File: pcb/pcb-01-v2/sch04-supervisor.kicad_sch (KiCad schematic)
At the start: 22 parts, among them J5 B5B-PH-K-S(LF)(SN), Q4 BC847BDW1T1G, SW1 PTS645SK43SMTR92LFS, SW2 PTS645SK43SMTR92LFS, U12 TMP1075DGKR, U2 ESP32-C6-WROOM-1-N8

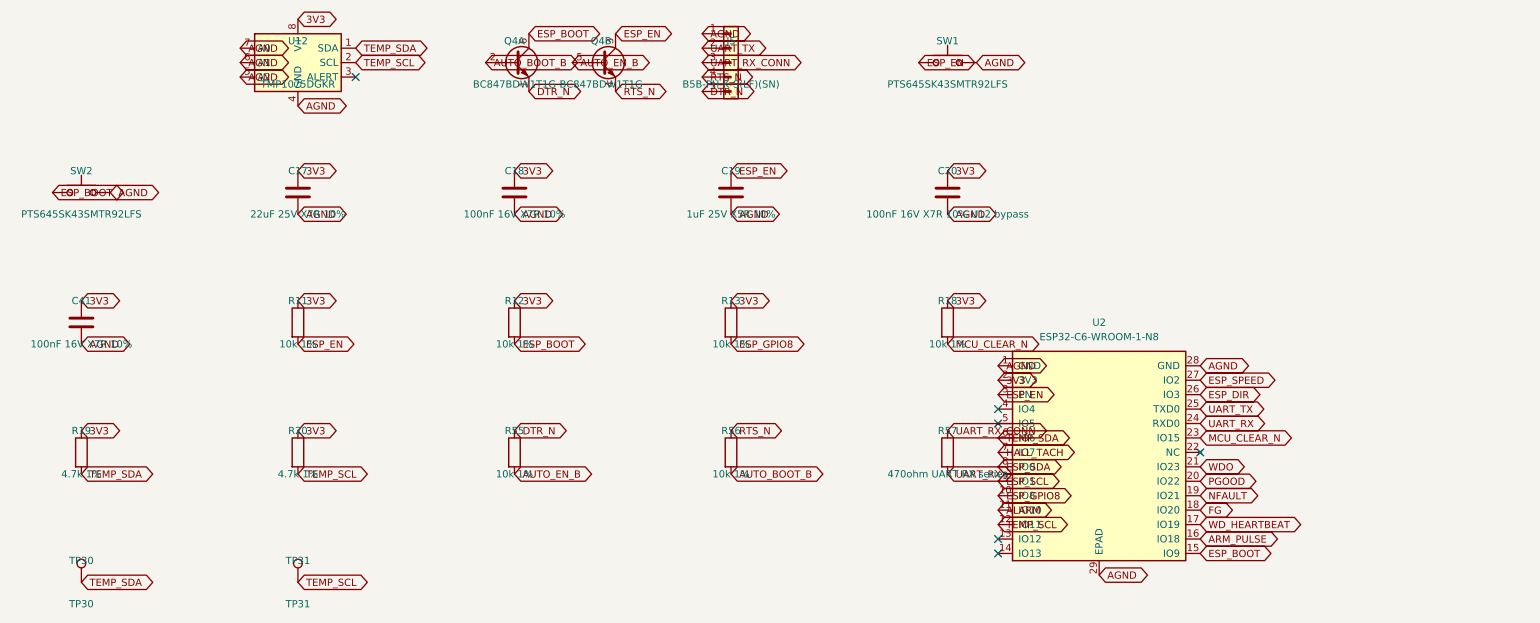
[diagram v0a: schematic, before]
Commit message: Redesign PCB-01 V2 for native USB-C
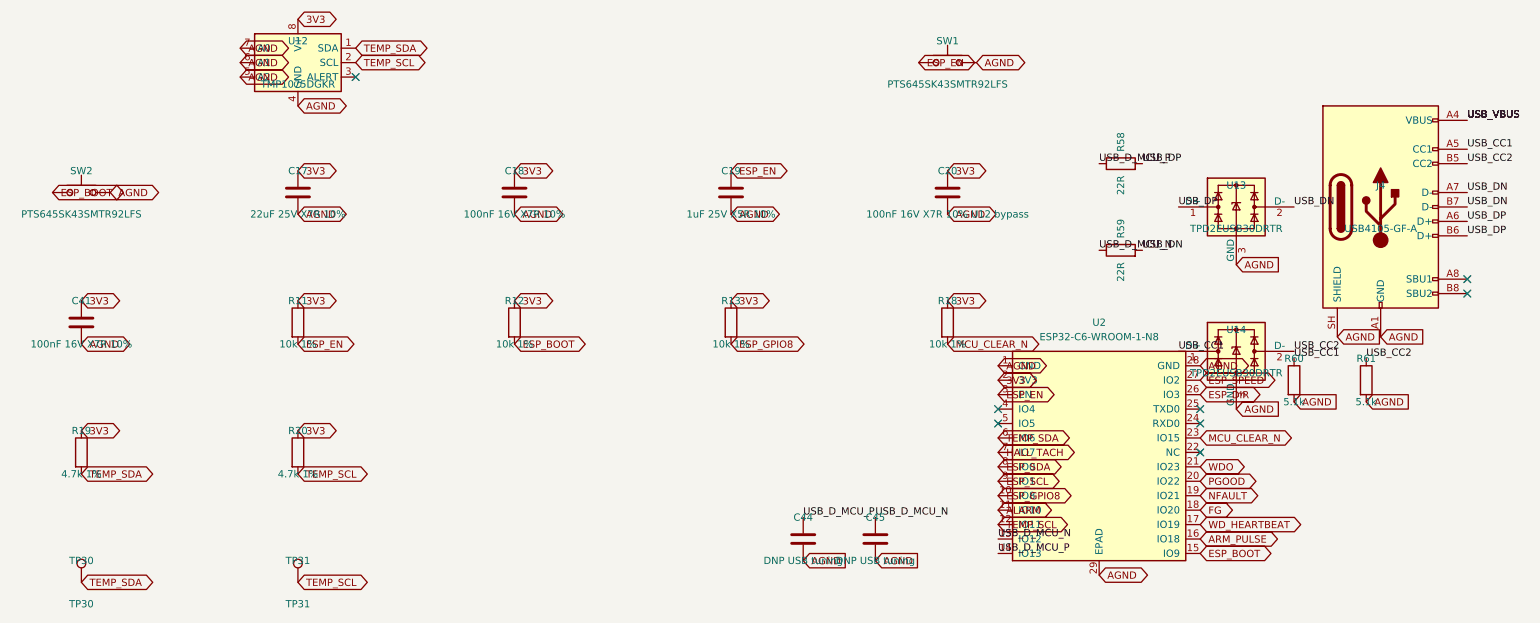
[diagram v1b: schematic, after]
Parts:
- removed J5: B5B-PH-K-S(LF)(SN), Connector_JST:JST_PH_B5B-PH-K_1x05_P2.00mm_Vertical, symbol Connector_Generic:Conn_01x05
- removed Q4: BC847BDW1T1G, symbol Transistor_BJT:BC847BDW1
- removed R55, R56: 10k 1%, Resistor_SMD:R_0402_1005Metric, symbol Device:R
- removed R57: 470ohm UART RX series, Resistor_SMD:R_0402_1005Metric, symbol Device:R
- added C44, C45: DNP USB tuning, Capacitor_SMD:C_0402_1005Metric, symbol Device:C
- added J4: USB4105-GF-A, Connector_USB:USB_C_Receptacle_GCT_USB4105-xx-A_16P_TopMnt_Horizontal, symbol Connector:USB_C_Receptacle_USB2.0_16P
- added R58, R59: 22R, Resistor_SMD:R_0402_1005Metric, symbol Device:R
- added R60, R61: 5.1k, Resistor_SMD:R_0402_1005Metric, symbol Device:R
- added U13, U14: TPD2EUSB30DRTR, Package_TO_SOT_SMD:Texas_DRT-3, symbol Power_Protection:TPD2EUSB30
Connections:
- net AGND: now also C44.2, C45.2, J4.A1 (GND), J4.A12 (GND), J4.B1 (GND), J4.B12 (GND), J4.SH (SHIELD), R60.2, R61.2, U13.3 (GND), U14.3 (GND)
- net USB_D_MCU_N: now reaches U2.13 (IO12)
- net USB_D_MCU_N: now also C45.1, R59.1
- net USB_D_MCU_P: now reaches U2.14 (IO13)
- net USB_D_MCU_P: now also C44.1, R58.1
- net UART_RX: no longer names the net of U2.24 (RXD0)
- net UART_TX: no longer names the net of U2.25 (TXD0)
- new net USB_CC1: J4.A5 (CC1), R60.1, U14.1 (D+)
- new net USB_CC2: J4.B5 (CC2), R61.1, U14.2 (D-)
- new net USB_DN: J4.A7 (D-), J4.B7 (D-), R59.2, U13.2 (D-)
- new net USB_DP: J4.A6 (D+), J4.B6 (D+), R58.2, U13.1 (D+)
- new net USB_VBUS: J4.A4 (VBUS), J4.A9 (VBUS), J4.B4 (VBUS), J4.B9 (VBUS)
- no-connect marks 6 -> 8
